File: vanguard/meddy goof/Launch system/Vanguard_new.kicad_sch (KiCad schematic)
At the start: 94 parts, among them J1 USB_C_Receptacle_USB2.0_16P, J2 Micro_SD_Card_Det1, J3 Conn_02x03_Odd_Even, J4 Conn_01x03, J5 Conn_01x03, J6 Conn_01x03, J7 Conn_01x02_Pin, Q4 BSS138, U1 TPS82130, U10 ATmega4809-A, U12 AP2112K-3.3, U3 ATSAMD11D14A-M, U4 BMP390L, U5 BD1020HFV-TR, U6 AT25DF641A-SH-T, U8 BNO055, U9 TPS61092, Y1 Crystal

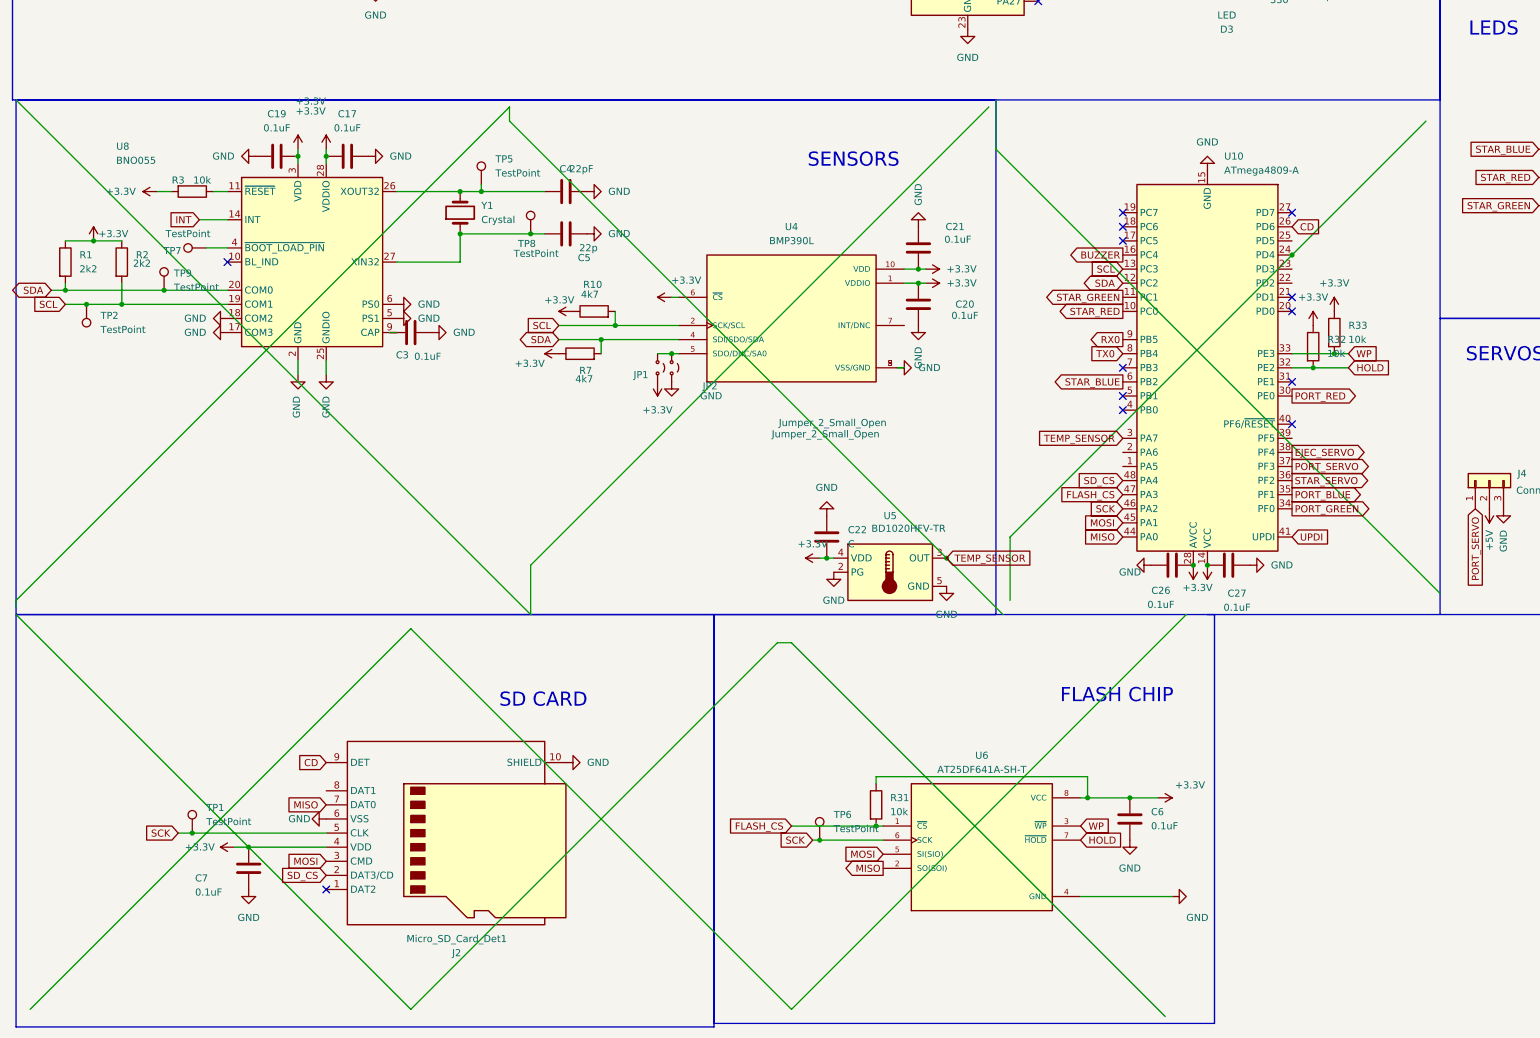
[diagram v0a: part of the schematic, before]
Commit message: wiring done
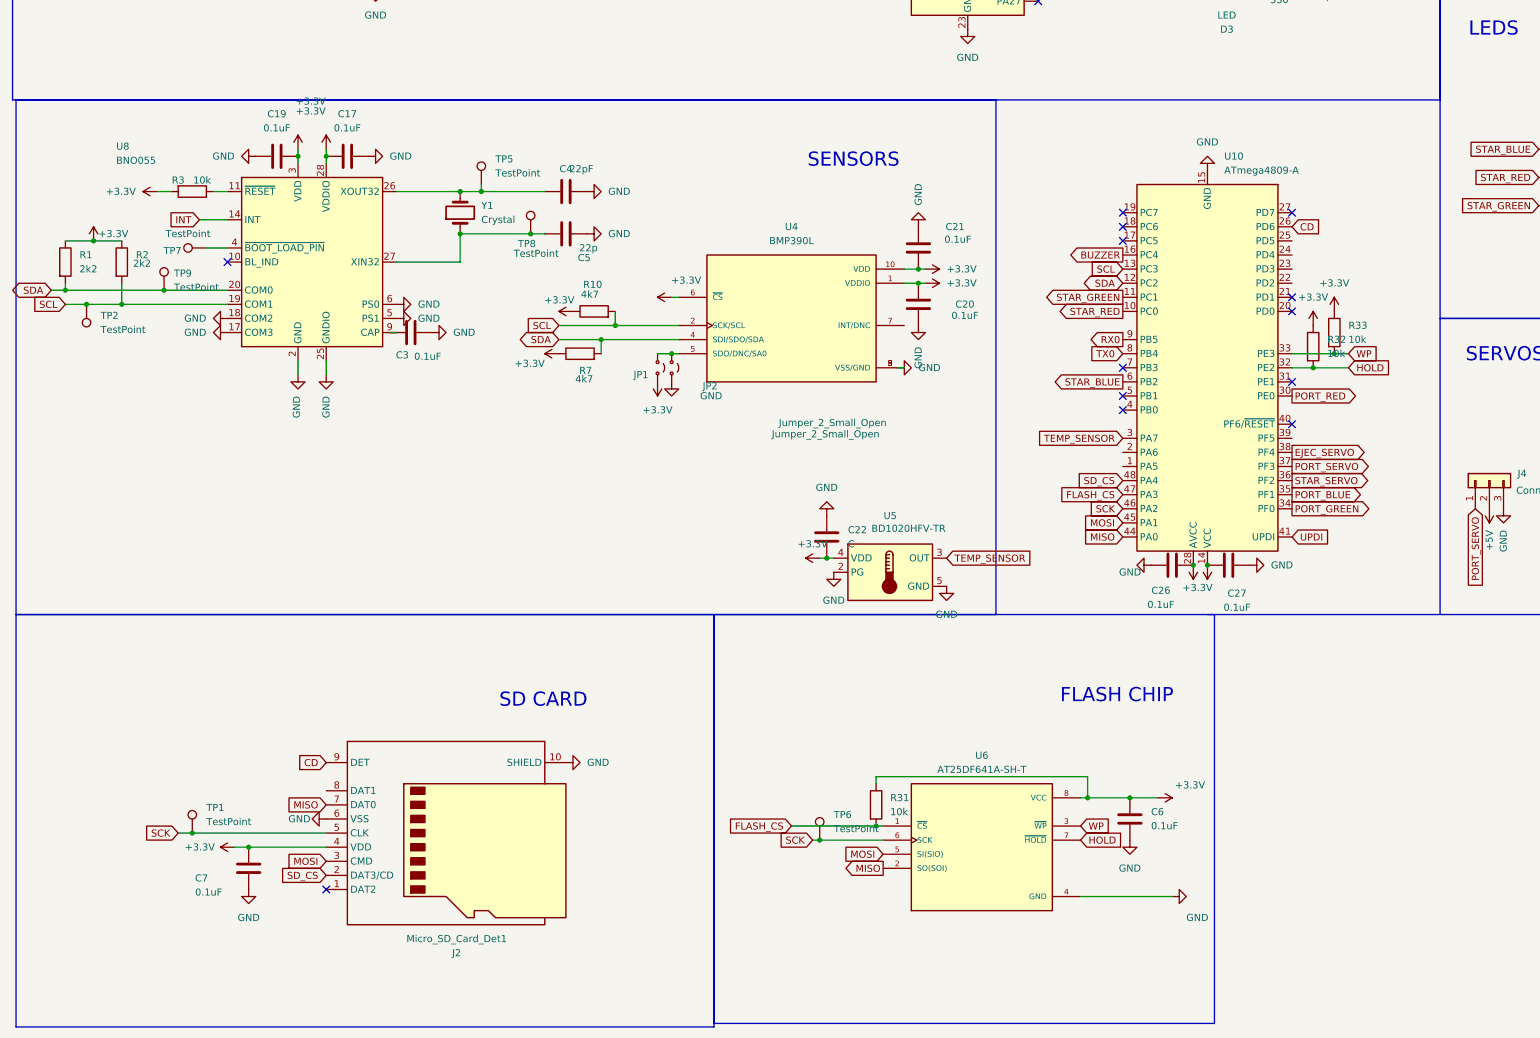
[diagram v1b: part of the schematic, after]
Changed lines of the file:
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@@
-	)
-	(junction
-		(at 180.34 182.88)
-		(diameter 0)
-		(color 0 0 0 0)
 	)
 	(junction
@@
 	)
 	(junction
-		(at 242.57 128.27)
-		(diameter 0)
-		(color 0 0 0 0)
-	)
-	(junction
 		(at 167.64 231.14)
 		(diameter 0)
@@
 	(wire
 		(pts
-			(xy 191.77 190.5) (xy 191.77 179.07)
-		)
-		(stroke
-			(width 0)
-			(type default)
-		)
-	)
-	(wire
-		(pts
 			(xy 168.91 52.07) (xy 171.45 52.07)
 		)
@@
 	(wire
 		(pts
-			(xy 149.86 198.12) (xy 152.4 198.12)
-		)
-		(stroke
-			(width 0)
-			(type default)
-		)
-	)
-	(wire
-		(pts
 			(xy 356.87 167.64) (xy 344.17 167.64)
 		)
@@
 	(wire
 		(pts
-			(xy 152.4 198.12) (xy 219.71 265.43)
-		)
-		(stroke
-			(width 0)
-			(type default)
-		)
-	)
-	(wire
-		(pts
 			(xy 339.09 162.56) (xy 349.25 162.56)
 		)
@@
 	(wire
 		(pts
-			(xy 12.7 190.5) (xy 101.6 101.6)
-		)
-		(stroke
-			(width 0)
-			(type default)
-		)
-	)
-	(wire
-		(pts
 			(xy 205.74 222.25) (xy 205.74 226.06)
 		)
@@
 	(wire
 		(pts
-			(xy 12.7 191.77) (xy 12.7 190.5)
-		)
-		(stroke
-			(width 0)
-			(type default)
-		)
-	)
-	(wire
-		(pts
 			(xy 63.5 147.32) (xy 63.5 149.86)
 		)
@@
 	(wire
 		(pts
-			(xy 242.57 128.27) (xy 266.7 104.14)
-		)
-		(stroke
-			(width 0)
-			(type default)
-		)
-	)
-	(wire
-		(pts
 			(xy 218.44 226.06) (xy 213.36 226.06)
 		)
@@
 	(wire
 		(pts
-			(xy 152.4 264.16) (xy 223.52 193.04)
-		)
-		(stroke
-			(width 0)
-			(type default)
-		)
-	)
-	(wire
-		(pts
 			(xy 171.45 46.99) (xy 170.18 46.99)
 		)
@@
 	(wire
 		(pts
-			(xy 191.77 179.07) (xy 242.57 128.27)
-		)
-		(stroke
-			(width 0)
-			(type default)
-		)
-	)
-	(wire
-		(pts
 			(xy 111.76 38.1) (xy 121.92 38.1)
 		)
@@
 	(wire
 		(pts
-			(xy 15.24 264.16) (xy 83.82 195.58)
-		)
-		(stroke
-			(width 0)
-			(type default)
-		)
-	)
-	(wire
-		(pts
 			(xy 146.05 40.64) (xy 166.37 40.64)
 		)
@@
 	(wire
 		(pts
-			(xy 83.82 195.58) (xy 152.4 264.16)
-		)
-		(stroke
-			(width 0)
-			(type default)
-		)
-	)
-	(wire
-		(pts
 			(xy 172.72 133.35) (xy 175.26 133.35)
 		)
@@
 	(wire
 		(pts
-			(xy 105.41 193.04) (xy 105.41 184.15)
-		)
-		(stroke
-			(width 0)
-			(type default)
-		)
-	)
-	(wire
-		(pts
 			(xy 335.28 40.64) (xy 342.9 40.64)
 		)
@@
 	(wire
 		(pts
-			(xy 189.23 100.33) (xy 189.23 109.22)
-		)
-		(stroke
-			(width 0)
-			(type default)
-		)
-	)
-	(wire
-		(pts
 			(xy 389.89 154.94) (xy 381 154.94)
 		)
@@
 	(wire
 		(pts
-			(xy 54.61 234.95) (xy 83.82 264.16)
-		)
-		(stroke
-			(width 0)
-			(type default)
-		)
-	)
-	(wire
-		(pts
 			(xy 212.09 62.23) (xy 215.9 62.23)
 		)
@@
 	(wire
 		(pts
-			(xy 101.6 104.14) (xy 180.34 182.88)
-		)
-		(stroke
-			(width 0)
-			(type default)
-		)
-	)
-	(wire
-		(pts
 			(xy 92.71 129.54) (xy 92.71 124.46)
 		)
@@
 	(wire
 		(pts
-			(xy 180.34 182.88) (xy 190.5 193.04)
-		)
-		(stroke
-			(width 0)
-			(type default)
-		)
-	)
-	(wire
-		(pts
 			(xy 381 154.94) (xy 377.19 154.94)
 		)
@@
 	(wire
 		(pts
-			(xy 83.82 264.16) (xy 149.86 198.12)
-		)
-		(stroke
-			(width 0)
-			(type default)
-		)
-	)
-	(wire
-		(pts
 			(xy 167.64 72.39) (xy 167.64 54.61)
 		)
@@
 	(wire
 		(pts
-			(xy 12.7 193.04) (xy 54.61 234.95)
-		)
-		(stroke
-			(width 0)
-			(type default)
-		)
-	)
-	(wire
-		(pts
 			(xy 92.71 52.07) (xy 116.84 52.07)
 		)
@@
 	(wire
 		(pts
-			(xy 12.7 100.33) (xy 105.41 193.04)
-		)
-		(stroke
-			(width 0)
-			(type default)
-		)
-	)
-	(wire
-		(pts
 			(xy 349.25 165.1) (xy 356.87 165.1)
 		)
@@
 	(wire
 		(pts
-			(xy 189.23 109.22) (xy 269.24 189.23)
-		)
-		(stroke
-			(width 0)
-			(type default)
-		)
-	)
-	(wire
-		(pts
 			(xy 382.27 102.87) (xy 382.27 105.41)
 		)
@@
 	(wire
 		(pts
-			(xy 101.6 101.6) (xy 101.6 104.14)
-		)
-		(stroke
-			(width 0)
-			(type default)
-		)
-	)
-	(wire
-		(pts
 			(xy 21.59 137.16) (xy 25.4 137.16)
 		)
@@
 		)
 		(stroke
-			(width 0)
-			(type default)
-		)
-	)
-	(wire
-		(pts
-			(xy 105.41 184.15) (xy 187.96 101.6)
-		)
-		(stroke

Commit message: fixed drc, the rest is bs
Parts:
- removed BZ1: Buzzer, Buzzer_Beeper:MagneticBuzzer_Kingstate_KCG0601, symbol Device:Buzzer
- removed D7, D8: SMLVN6RGB, LED_SMD:LED_ROHM_SMLVN6, symbol LED:SMLVN6RGB
- removed Q4: BSS138, Package_TO_SOT_SMD:SOT-23, symbol Transistor_FET:BSS138
- removed R21, R22, R23, R24, R25, R26: 220, Resistor_SMD:R_0603_1608Metric, symbol Device:R
- removed R34: 2k2, Resistor_SMD:R_0603_1608Metric, symbol Device:R

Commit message: added power switch
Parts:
- removed C12: 2u2, Capacitor_SMD:C_0603_1608Metric, symbol Device:C
- removed C13: 100u, Capacitor_SMD:C_0603_1608Metric, symbol Device:C_Polarized_US
- removed C17, C19: 0.1uF, Capacitor_SMD:C_0603_1608Metric, symbol Device:C
- removed C22: C, Capacitor_SMD:C_0603_1608Metric, symbol Device:C
- removed C5: 22p, Capacitor_SMD:C_0603_1608Metric, symbol Device:C
- removed C8: 10u, Capacitor_SMD:C_0603_1608Metric, symbol Device:C
- removed J4, J5, J6: Conn_01x03, Connector_PinHeader_2.54mm:PinHeader_1x03_P2.54mm_Vertical, symbol Connector_Generic:Conn_01x03
- removed J7: Conn_01x02_Pin, Connector_JST:JST_PH_B2B-PH-K_1x02_P2.00mm_Vertical, symbol Connector:Conn_01x02_Pin
- removed L1: SLF7055T-6R8N2R8-3PF, Inductor_SMD:L_7.3x7.3_H4.5, symbol SLF7055T-6R8N2R8-3PF[1]:SLF7055T-6R8N2R8-3PF
- removed R27, R28, R30: 100k, Resistor_SMD:R_0603_1608Metric, symbol Device:R
- removed R29: 315k, Resistor_SMD:R_0603_1608Metric, symbol Device:R
- removed TP2, TP5, TP7, TP8, TP9: TestPoint, TestPoint:TestPoint_Pad_1.0x1.0mm, symbol Connector:TestPoint
- removed U5: BD1020HFV-TR, Package_TO_SOT_SMD:HVSOF5, symbol Sensor_Temperature:BD1020HFV
- removed U8: BNO055, Package_LGA:LGA-28_5.2x3.8mm_P0.5mm, symbol Sensor_Motion:BNO055
- removed U9: TPS61092, Package_DFN_QFN:Texas_RSA_VQFN-16-1EP_4x4mm_P0.65mm_EP2.7x2.7mm_ThermalVias, symbol Regulator_Switching:TPS61092
- removed Y1: Crystal, Crystal:Crystal_C26-LF_D2.1mm_L6.5mm_Vertical, symbol Device:Crystal
- added BZ1: Buzzer, Buzzer_Beeper:MagneticBuzzer_Kingstate_KCG0601, symbol Device:Buzzer
- added BZ2: Buzzer, symbol Device:Buzzer
- added D4, D6: LED, symbol Device:LED
- added J5: igniter, symbol Connector:Conn_01x02_Pin
- added JP3: SolderJumper_2_Open, symbol Jumper:SolderJumper_2_Open
- added Q4: BSS138, Package_TO_SOT_SMD:SOT-23, symbol Transistor_FET:BSS138
- added R14: 4k7, Resistor_SMD:R_0603_1608Metric, symbol Device:R
- added R15: R, symbol Device:R
- added R16, R17: 10k, symbol Device:R
- added R34: 2k2, Resistor_SMD:R_0603_1608Metric, symbol Device:R
- added SW1: LAUNCH, symbol Switch:SW_Push
- added SW2: POWER, symbol Switch:SW_SPDT
- added SW4: SW_SPST, symbol Switch:SW_SPST
- added U2: SHT31-DIS, Sensor_Humidity:Sensirion_DFN-8-1EP_2.5x2.5mm_P0.5mm_EP1.1x1.7mm, symbol Sensor_Humidity:SHT31-DIS
- C3: footprint Capacitor_SMD:C_0603_1608Metric -> (none)
- C4: value 22pF -> 10uF; footprint Capacitor_SMD:C_0603_1608Metric -> (none)
- R1, R2: value 2k2 -> 10k; footprint Resistor_SMD:R_0603_1608Metric -> (none)
- R3: value 10k -> R; footprint Resistor_SMD:R_0603_1608Metric -> (none)
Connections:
- net +3.3V: now also C3.1, C4.1, R10.2, BZ1.1 (+), JP3.1 (A), R14.2, U2.5 (VDD); no longer R10.1, R2.1, R3.2
- net BUZZER: now also Q4.1 (G), R34.1
- net GND: now also R2.2, BZ2.2 (-), D4.1 (K), D6.1 (K), Q4.2 (S), R16.1, R17.1, R34.2, U2.7 (R), U2.8 (VSS), U2.9 (VSS); no longer C3.2, C4.2
- net SCL: now also R14.1, U2.4 (SCL); no longer R10.2, R2.2
- net SDA: now also R10.1, U2.1 (SDA); no longer R1.2
- net VBUS: now also J5.2 (Pin_2), SW2.3 (C); no longer J1.A4 (VBUS), J1.A9 (VBUS), J1.B4 (VBUS), J1.B9 (VBUS)
- net at R3.1: now also J5.1 (Pin_1), SW4.1 (A)
- net RECORD: now reaches U10.18 (PC6)
- net RECORD: now also R15.1, R17.2, SW1.1, SW4.2 (B)
- net EJEC_SERVO: no longer names the net of U10.38 (PF4)
- net PORT_SERVO: no longer names the net of U10.37 (PF3)
- net STAR_SERVO: no longer names the net of U10.36 (PF2)
- net TEMP_SENSOR: no longer names the net of U10.3 (PA7)
- new net: BZ1.2 (-), Q4.3 (D)
- new net: D6.2 (A), R15.2
- new net: JP3.2 (B), R2.1, U2.2 (ADDR)
- new net: R1.2, U2.6 (~{RESET})
- new net: D4.2 (A), R3.2
- new net: BZ2.1 (+), SW1.2
- new net: R16.2, SW2.1 (A)
- new net P_IN: J1.A4 (VBUS), J1.A9 (VBUS), J1.B4 (VBUS), J1.B9 (VBUS), SW2.2 (B)
- no-connect marks 28 -> 26
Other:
- note removed: "SERVO POWER"
- note removed: "SERVOS"
- moved on the sheet: C1, C20, C21, JP1, JP2, R10, R7, U4

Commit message: finished everything
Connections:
- net P_IN is gone; now on net VBUS: J1.A4 (VBUS), J1.A9 (VBUS), J1.B4 (VBUS), J1.B9 (VBUS), SW2.2 (B)
- net VBUS: no longer D12.2 (A), J5.2 (Pin_2), SW2.3 (C)
- new net pwr: D12.2 (A), J5.2 (Pin_2), SW2.3 (C)
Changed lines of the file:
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@@
 	(wire
 		(pts
-			(xy 97.79 38.1) (xy 101.6 38.1)
-		)
-		(stroke
-			(width 0)
-			(type default)
-		)
-	)
-	(wire
-		(pts
 			(xy 212.09 74.93) (xy 228.6 74.93)
 		)
@@
 	(wire
 		(pts
-			(xy 316.23 157.48) (xy 314.96 158.75)
+			(xy 314.96 157.48) (xy 320.04 157.48)
 		)
 		(stroke
@@
 	(wire
 		(pts
+			(xy 276.86 40.64) (xy 283.21 40.64)
+		)
+		(stroke
+			(width 0)
+			(type default)
+		)
+	)
+	(wire
+		(pts
 			(xy 158.75 129.54) (xy 158.75 130.81)
 		)
@@
 	(wire
 		(pts
-			(xy 320.04 157.48) (xy 316.23 157.48)
-		)
-		(stroke
-			(width 0)
-			(type default)
-		)
-	)
-	(wire
-		(pts
 			(xy 165.1 33.02) (xy 201.93 33.02)
 		)
@@
 	(wire
 		(pts
-			(xy 92.71 38.1) (xy 93.98 38.1)
+			(xy 92.71 38.1) (xy 101.6 38.1)
 		)
 		(stroke
@@
 		)
 	)
-	(global_label "CD"
+	(global_label "pwr"
 		(shape input)
-		(at 242.57 123.19 0)
+		(at 336.55 160.02 90)
 		(fields_autoplaced yes)
 		(effects
@@
 		)
 		(property "Intersheetrefs" "${INTERSHEET_REFS}"
-			(at 248.0952 123.19 0)
+			(at 336.55 153.7691 90)
 			(effects
 				(font
@@
 		)
 	)
-	(global_label "P_IN"
+	(global_label "CD"
 		(shape input)
-		(at 93.98 38.1 90)
+		(at 242.57 123.19 0)
 		(fields_autoplaced yes)
 		(effects
@@
 		)
 		(property "Intersheetrefs" "${INTERSHEET_REFS}"
-			(at 93.98 30.9419 90)
+			(at 248.0952 123.19 0)
 			(effects
 				(font
@@
 		)
 	)
-	(global_label "P_OUT"
-		(shape input)
-		(at 97.79 38.1 90)
-		(fields_autoplaced yes)
-		(effects
-			(font
-				(size 1.27 1.27)
-			)
-			(justify left)
-		)
-		(property "Intersheetrefs" "${INTERSHEET_REFS}"
-			(at 97.79 29.2486 90)
-			(effects
-				(font
-					(size 1.27 1.27)
-				)
-				(justify left)
-				(hide yes)
-			)
-		)
-	)
 	(global_label "HOLD"
 		(shape input)
@@
 		)
 	)
-	(global_label "P_IN"
-		(shape input)
-		(at 314.96 158.75 90)
-		(fields_autoplaced yes)
-		(effects
-			(font
-				(size 1.27 1.27)
-			)
-			(justify left)
-		)
-		(property "Intersheetrefs" "${INTERSHEET_REFS}"
-			(at 314.96 151.5919 90)
-			(effects
-				(font
-					(size 1.27 1.27)
-				)
-				(justify left)
-				(hide yes)
-			)
-		)
-	)
 	(global_label "STAR_RED"
 		(shape output)
@@
 		)
 	)
+	(global_label "pwr"
+		(shape input)
+		(at 276.86 40.64 90)
+		(fields_autoplaced yes)
+		(effects
+			(font
+				(size 1.27 1.27)
+			)
+			(justify left)
+		)
+		(property "Intersheetrefs" "${INTERSHEET_REFS}"
+			(at 276.86 34.3891 90)
+			(effects
+				(font
+					(size 1.27 1.27)
+				)
+				(justify left)
+				(hide yes)
+			)
+		)
+	)
 	(global_label "UPDI"
 		(shape output)
@@
 		)
 	)
-	(global_label "P_OUT"
-		(shape input)
-		(at 337.82 160.02 90)
-		(fields_autoplaced yes)
-		(effects
-			(font
-				(size 1.27 1.27)
-			)
-			(justify left)
-		)
-		(property "Intersheetrefs" "${INTERSHEET_REFS}"
-			(at 337.82 151.1686 90)
-			(effects
-				(font
-					(size 1.27 1.27)
-				)
-				(justify left)
-				(hide yes)
-			)
-		)
-	)
 	(global_label "RX0"
 		(shape output)
@@
 	)
 	(symbol
+		(lib_id "power:VBUS")
+		(at 314.96 157.48 90)
+		(unit 1)
+		(exclude_from_sim no)
+		(in_bom yes)
+		(on_board yes)
+		(dnp no)
+		(fields_autoplaced yes)
+		(property "Reference" "#PWR030"
+			(at 318.77 157.48 0)
+			(effects
+				(font
+					(size 1.27 1.27)
+				)
+				(hide yes)
+			)
+		)
+		(property "Value" "VBUS"
+			(at 311.15 157.4799 90)
+			(effects
+				(font
+					(size 1.27 1.27)
+				)
+				(justify left)
+			)
+		)
+		(property "Footprint" ""
+			(at 314.96 157.48 0)
+			(effects
+				(font
+					(size 1.27 1.27)
+				)
+				(hide yes)
+			)
+		)
+		(property "Datasheet" ""
+			(at 314.96 157.48 0)
+			(effects
+				(font
+					(size 1.27 1.27)
+				)
+				(hide yes)
+			)
+		)
+		(property "Description" "Power symbol creates a global label with name \"VBUS\""
+			(at 314.96 157.48 0)
+			(effects
+				(font
+					(size 1.27 1.27)
+				)
+				(hide yes)
+			)
+		)
+		(pin "1"
+		)
+		(instances
+			(project ""
+				(path "/972fbf12-2dcd-4fdf-b1c9-8a2880c46640"
+					(reference "#PWR030")
+					(unit 1)
+				)
+			)
+		)
+	)
+	(symbol
 		(lib_id "power:+3.3V")
 		(at 127 133.35 90)
@@
 					(unit 1)
 				)
-			)
-		)
-	)
-	(symbol
-		(lib_id "power:VBUS")
-		(at 283.21 40.64 90)
-		(unit 1)
-		(exclude_from_sim no)
-		(in_bom yes)
-		(on_board yes)
-		(dnp no)
-		(fields_autoplaced yes)
-		(property "Reference" "#PWR0130"
-			(at 287.02 40.64 0)
-			(effects
-				(font
-					(size 1.27 1.27)
-				)
-				(hide yes)
-			)
-		)
-		(property "Value" "VBUS"
-			(at 279.4 40.6399 90)
-			(effects
-				(font
-					(size 1.27 1.27)
-				)
-				(justify left)
-			)
-		)
-		(property "Footprint" ""
-			(at 283.21 40.64 0)
-			(effects
-				(font
-					(size 1.27 1.27)
-				)
-				(hide yes)
-			)
-		)
-		(property "Datasheet" ""
-			(at 283.21 40.64 0)
-			(effects
-				(font
-					(size 1.27 1.27)
-				)
-				(hide yes)
-			)
-		)
-		(property "Description" "Power symbol creates a global label with name \"VBUS\""
-			(at 283.21 40.64 0)
-			(effects
-				(font
-					(size 1.27 1.27)
-				)
-				(hide yes)
-			)
-		)
-		(pin "1"
-		)
-		(instances
-			(project "Vanguard_new"
-				(path "/972fbf12-2dcd-4fdf-b1c9-8a2880c46640"
-					(reference "#PWR0130")
-					(unit 1)
-				)
